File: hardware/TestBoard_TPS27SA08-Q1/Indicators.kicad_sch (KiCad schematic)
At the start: 21 parts

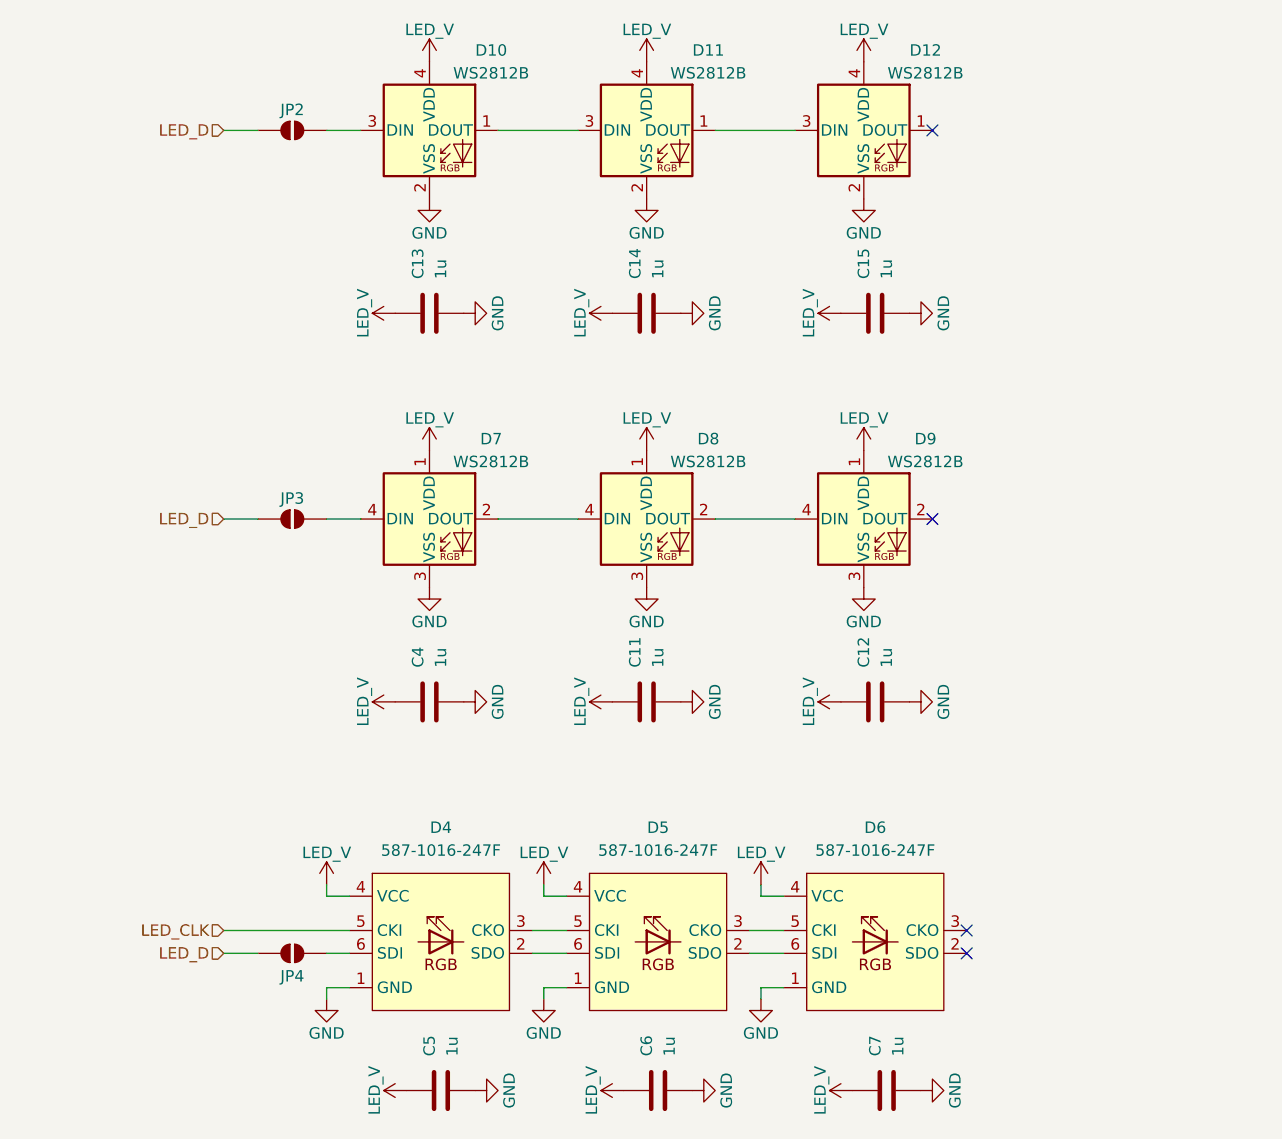
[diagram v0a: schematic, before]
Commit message: revisions (dip switch for address, leds on gpio outputs, logic analyzer pinout?, ...)
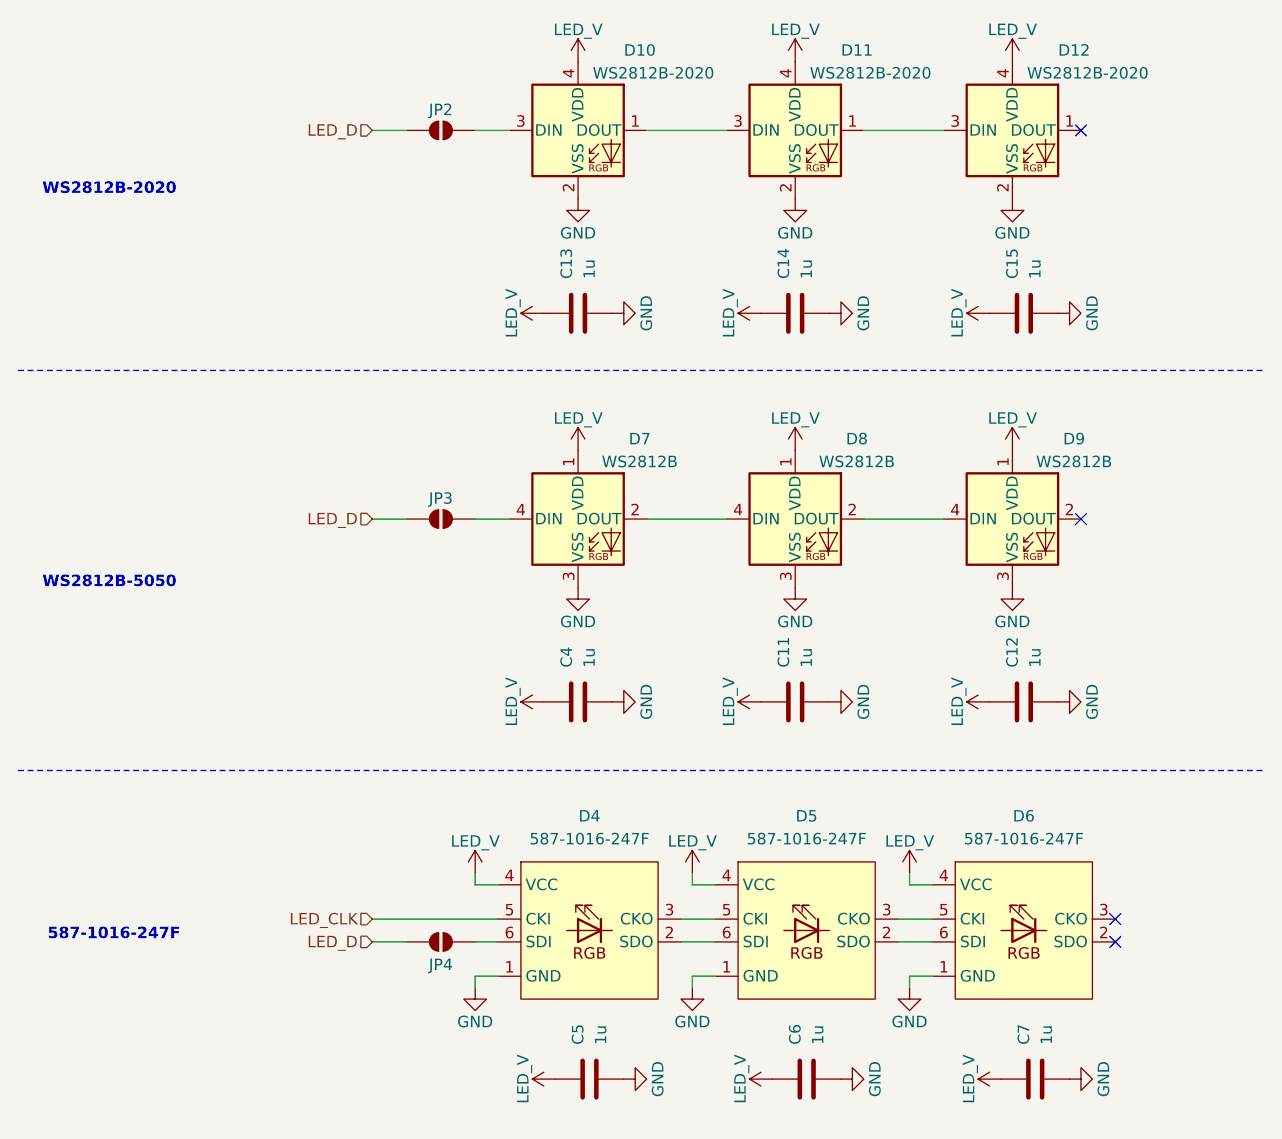
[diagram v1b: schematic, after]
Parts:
- D10, D11, D12: value WS2812B -> WS2812B-2020
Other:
- note added: "587-1016-247F"
- note added: "WS2812B-2020"
- note added: "WS2812B-5050"
- moved on the sheet: C11, C12, C13, C14, C15, C4, C5, C6, C7, D10, D11, D12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
